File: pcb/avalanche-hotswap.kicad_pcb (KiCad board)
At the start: 2 copper layers, 178.4 x 118.1 mm, 138 parts, among them J1 TRRS, J2 LED, J3 OLED, P1 i2c_pin, P2 i2c_pin, SW1 SW_Push, SW10 SW_Push, SW11 SW_Push, SW12 SW_Push, SW13 SW_Push, SW14 SW_Push, SW15 SW_Push, SW16 SW_Push, SW17 SW_Push, SW18 SW_Push, SW19 SW_Push, SW2 SW_Push, SW20 SW_Push, SW21 SW_Push, SW22 SW_Push, SW23 SW_Push, SW24 SW_Push, SW25 SW_Push, SW26 SW_Push, SW27 SW_Push, SW28 SW_Push, SW29 SW_Push, SW3 SW_Push, SW30 SW_Push, SW31 SW_Push, SW32 SW_Push, SW4 SW_Push, SW5 SW_Push, SW6 SW_Push, SW7 SW_Push, SW8 SW_Push, SW9 SW_Push, U1 ProMicro

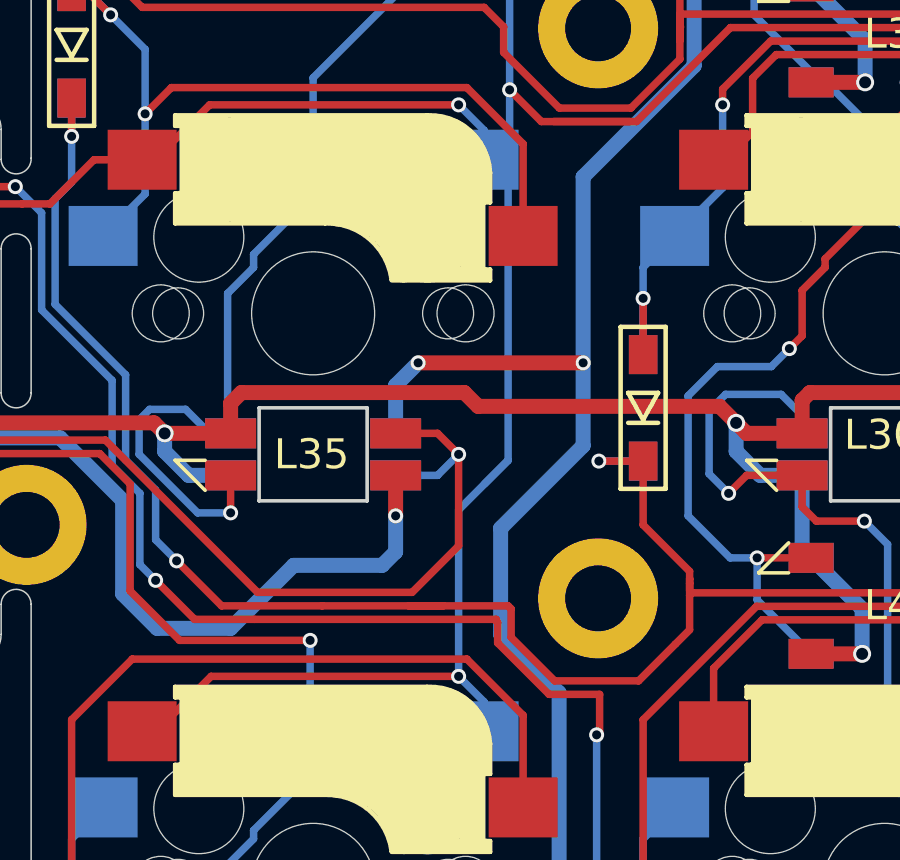
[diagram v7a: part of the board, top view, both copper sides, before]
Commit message: Fixed ground routing
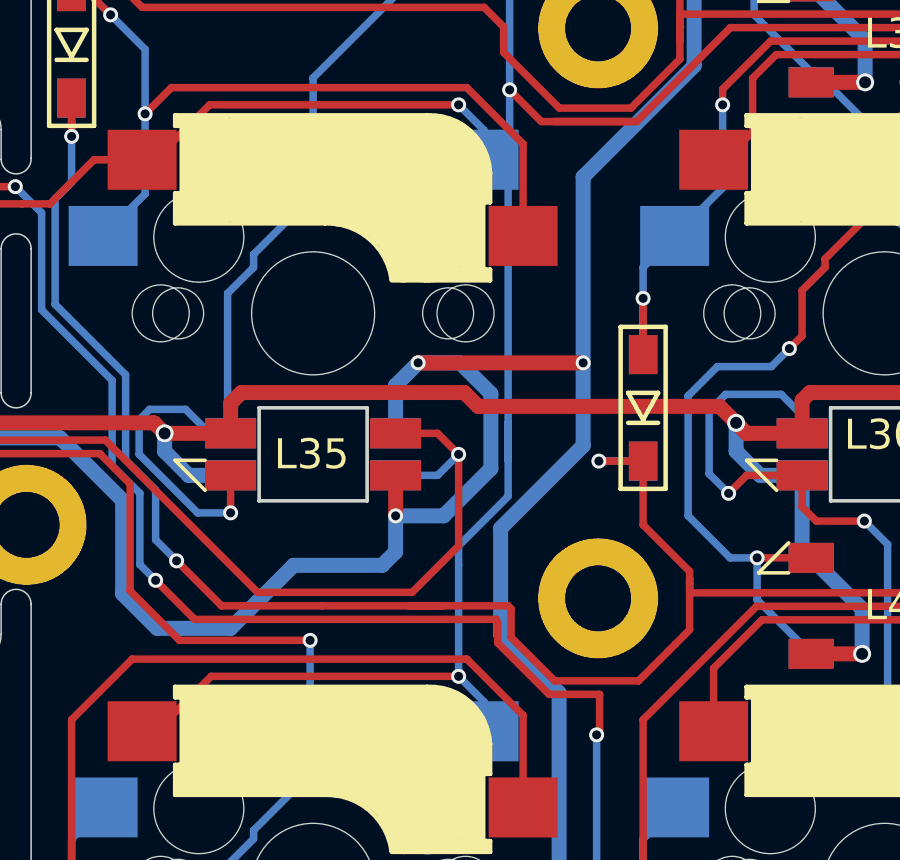
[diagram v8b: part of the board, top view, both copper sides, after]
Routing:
- net GND: track 1159.1 -> 1168.3 mm
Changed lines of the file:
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@@
     (thickness 1.6)
     (drawings 147)
-    (tracks 4133)
+    (tracks 4140)
     (zones 0)
     (modules 138)
@@
   (segment (start 107.75 91.5) (end 108.5 90.75) (width 0.5) (layer B.Cu) (net 27))
   (segment (start 107.75 93.1) (end 107.75 91.5) (width 0.5) (layer B.Cu) (net 27))
+  (segment (start 110.92499 91.77499) (end 110.92499 94.27501) (width 0.5) (layer B.Cu) (net 27))
+  (segment (start 109.35 95.85) (end 107.75 95.85) (width 0.5) (layer B.Cu) (net 27))
+  (segment (start 110.92499 94.27501) (end 109.35 95.85) (width 0.5) (layer B.Cu) (net 27))
+  (segment (start 109.9 90.75) (end 110.92499 91.77499) (width 0.5) (layer B.Cu) (net 27))
+  (segment (start 108.5 90.75) (end 109.9 90.75) (width 0.5) (layer B.Cu) (net 27))
   (segment (start 233.967426 69.726509) (end 244.120862 68.118362) (width 0.25) (layer F.Cu) (net 28) (status 10))
   (segment (start 247.889024 68.732194) (end 250.489676 68.320291) (width 0.25) (layer F.Cu) (net 28) (status 20))
@@
   (segment (start 110.7 83) (end 109.85 82.15) (width 0.25) (layer B.Cu) (net 45))
   (segment (start 110.7 83.98) (end 110.7 83) (width 0.25) (layer B.Cu) (net 45))
-  (segment (start 110.7 94.8) (end 111.5 94) (width 0.25) (layer B.Cu) (net 45))
   (segment (start 111.5 84.78) (end 110.7 83.98) (width 0.25) (layer B.Cu) (net 45))
-  (segment (start 111.5 94) (end 111.5 84.78) (width 0.25) (layer B.Cu) (net 45))
   (segment (start 99.3 103.03) (end 99.77 103.03) (width 0.25) (layer F.Cu) (net 45))
   (segment (start 101.6 101.2) (end 109.85 101.2) (width 0.25) (layer F.Cu) (net 45))
@@
   (segment (start 110.7 102.05) (end 109.85 101.2) (width 0.25) (layer B.Cu) (net 45))
   (segment (start 110.7 103.03) (end 110.7 102.05) (width 0.25) (layer B.Cu) (net 45))
-  (segment (start 109.85 95.65) (end 111.5 94) (width 0.25) (layer B.Cu) (net 45))
-  (segment (start 109.85 101.2) (end 109.85 95.65) (width 0.25) (layer B.Cu) (net 45))
   (segment (start 111.55 81.65) (end 111.55 83.13) (width 0.25) (layer B.Cu) (net 45) (status 20))
   (via (at 111.55 81.65) (size 0.5) (drill 0.3) (layers F.Cu B.Cu) (net 45))
@@
   (segment (start 111.18 64.93) (end 112.1 65.85) (width 0.25) (layer B.Cu) (net 45))
   (segment (start 110.7 64.93) (end 111.18 64.93) (width 0.25) (layer B.Cu) (net 45))
+  (segment (start 109.85 96.850812) (end 109.85 97.5) (width 0.25) (layer B.Cu) (net 45))
+  (segment (start 111.5 95.200812) (end 109.85 96.850812) (width 0.25) (layer B.Cu) (net 45))
+  (segment (start 111.5 92.75) (end 111.5 95.200812) (width 0.25) (layer B.Cu) (net 45))
+  (segment (start 111.5 94) (end 111.5 92.75) (width 0.25) (layer B.Cu) (net 45))
+  (segment (start 111.5 92.75) (end 111.5 84.78) (width 0.25) (layer B.Cu) (net 45))
+  (segment (start 109.85 101.2) (end 109.85 97.5) (width 0.25) (layer B.Cu) (net 45))
   (segment (start 118.35 45.88) (end 118.35 44.7) (width 0.25) (layer F.Cu) (net 46) (status 10))
   (segment (start 118.35 44.7) (end 119.55 43.5) (width 0.25) (layer F.Cu) (net 46))
